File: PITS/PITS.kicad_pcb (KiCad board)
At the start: 2 copper layers, 65 x 30 mm, 56 parts, among them P1 CONN_02X20, P10 I2C, P11 I2C, P12 I2C, P13 I2C, P14 BATT, P2 BNC, P3 BNC, P4 BNC, P5 BNC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

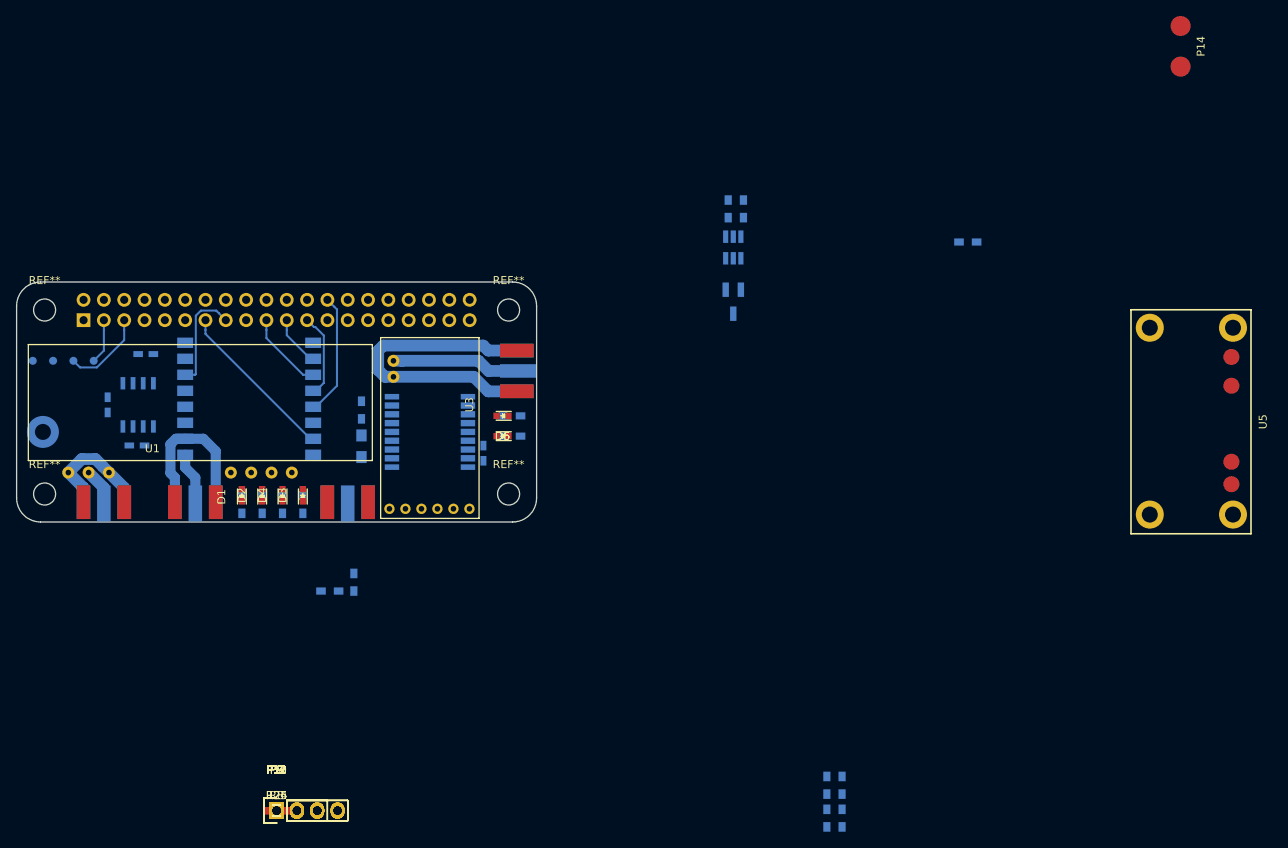
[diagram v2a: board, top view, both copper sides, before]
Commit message: layout - work in progress - power net
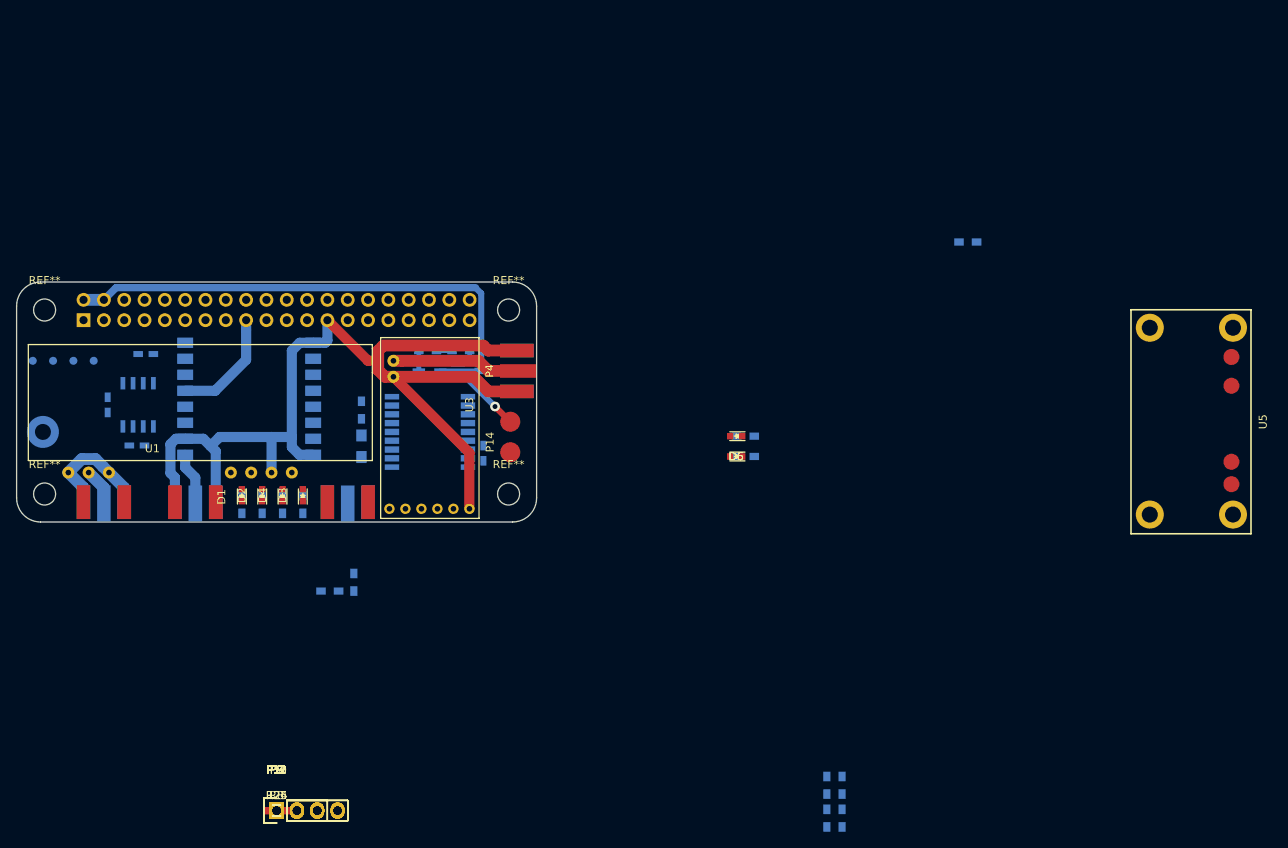
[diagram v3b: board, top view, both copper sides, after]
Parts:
- P14: footprint Connectors:SMD_2 -> Connectors:SMD_2_small
- P4: moved to F.Cu
- moved P14 94.8 mm to (116.7, 66.5), turned to 270 degrees
- moved R6 41.5 mm to (106.4, 57.6), turned to 0 degrees
- moved Q2 41.0 mm to (106.6, 60.1), turned to 0 degrees
- moved R19 39.5 mm to (110.5, 57.6), turned to 180 degrees
- moved Q1 34.1 mm to (111.6, 60.1), turned to 90 degrees
- moved D5 29.3 mm to (144.9, 70.8)
- moved R22 29.3 mm to (146.1, 70.8)
- moved D6 29.3 mm to (144.9, 68.3)
- moved R23 29.3 mm to (146.1, 68.3)
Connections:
- P14 pad 1: +BATT -> +5V_PSU
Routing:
- net GND: track 74.6 -> 143.2 mm
- net +5V: track 0.00 -> 65.5 mm
- net /GPIO27: track 20.6 -> 0.00 mm
- net /GPIO7(CE1): track 15.3 -> 0.00 mm
- net +3V3: track 0.00 -> 14.2 mm
- net /GPIO22: track 13.2 -> 0.00 mm
- net +5V_PSU: track 0.00 -> 11.0 mm, vias 0 -> 1
- net /GPIO3(SCL1): track 10.6 -> 0.00 mm
- net /GPIO11(SCLK0): track 10.6 -> 0.00 mm
- net /GPIO10(MOSI0): track 9.98 -> 0.00 mm
- net /GPIO9(MISO0): track 6.40 -> 0.00 mm
- net /GPIO2(SDA1): track 5.61 -> 0.00 mm
- net Net-(Q1-Pad2): track 0.00 -> 5.05 mm
- net Net-(Q2-Pad1): track 0.00 -> 3.49 mm

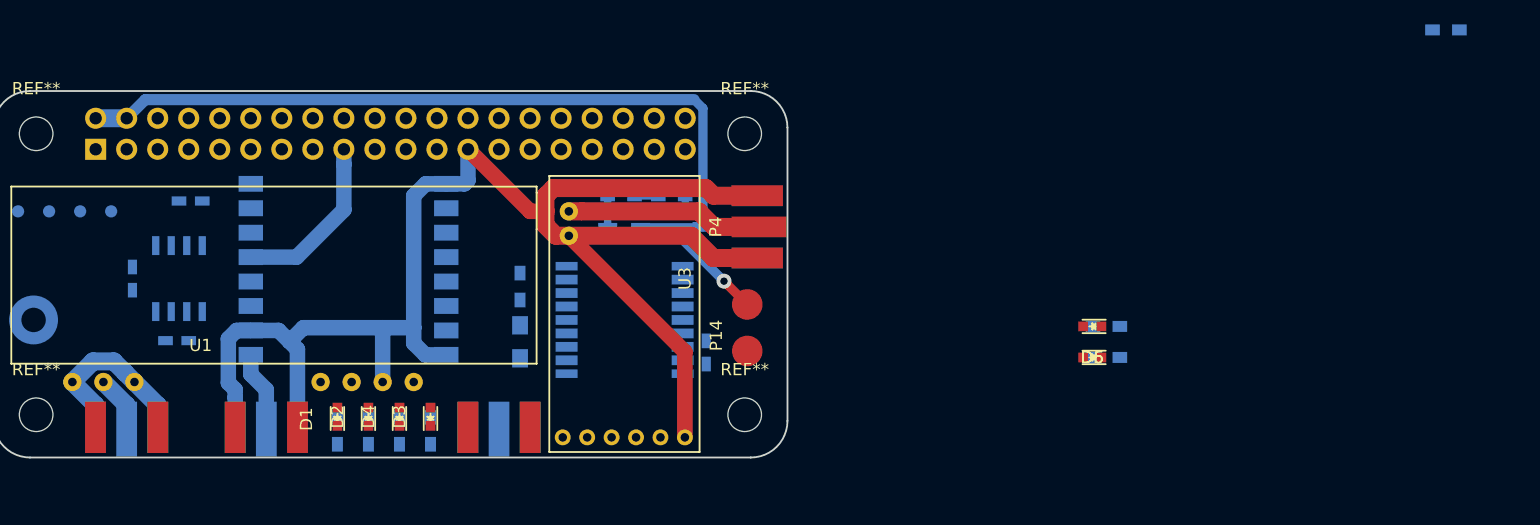
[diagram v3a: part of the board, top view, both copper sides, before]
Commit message: layout - work in progress - first digital nets
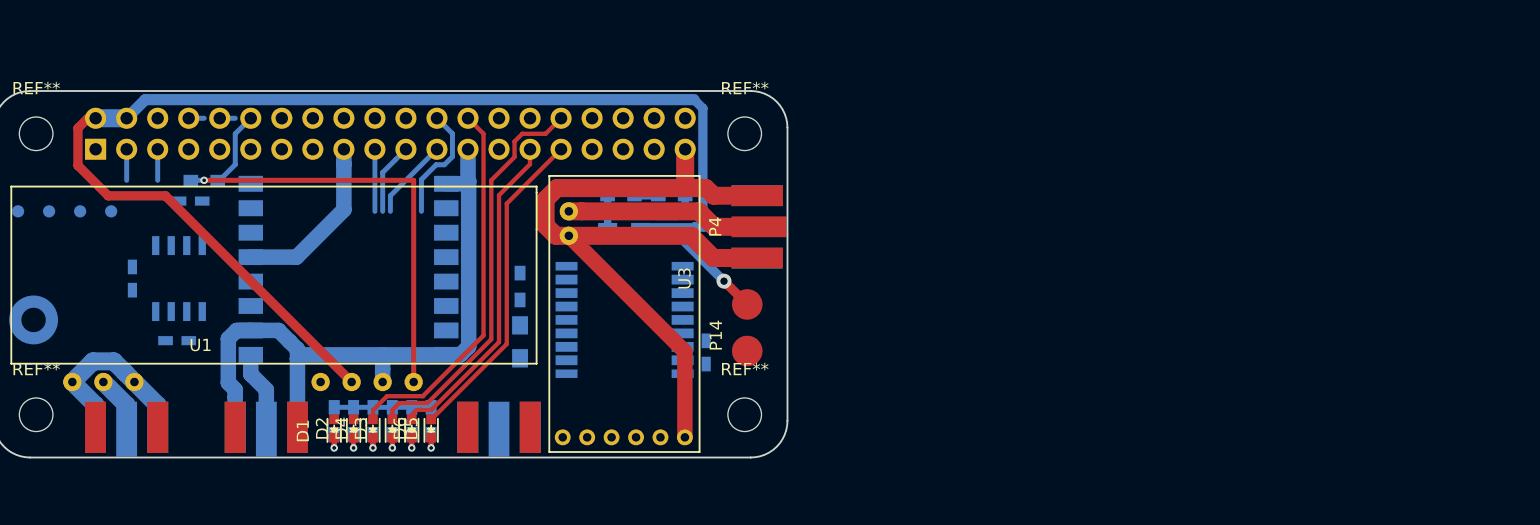
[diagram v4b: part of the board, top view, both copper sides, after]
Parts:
- moved R26 102.4 mm to (72.3, 56.3), turned to 180 degrees
- moved R22 57.1 mm to (89.2, 76.0), turned to 90 degrees
- moved D5 56.0 mm to (89.2, 76.6), turned to 90 degrees
- moved R23 55.8 mm to (90.8, 76.0), turned to 90 degrees
- moved D6 54.8 mm to (90.8, 76.6), turned to 90 degrees
- moved D3 3.27 mm to (87.7, 76.6)
- moved R20 3.23 mm to (87.7, 76.0)
- moved D4 2.38 mm to (86.1, 76.6)
- moved R21 2.32 mm to (86.1, 76.0)
- moved D2 1.56 mm to (84.5, 76.6)
- moved R15 1.47 mm to (84.5, 76.0)
- moved D1 1.01 mm to (82.9, 76.6)
- moved R14 0.86 mm to (82.9, 76.0)
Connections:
- D1 pad 1: GND -> /D1
- D1 pad 2: /D1 -> Net-(D1-Pad2)
- D2 pad 1: GND -> /D2
- D2 pad 2: /D2 -> Net-(D2-Pad2)
- D3 pad 1: GND -> /D3
- D3 pad 2: /D3 -> /GPIO12
- D4 pad 1: GND -> /D4
- D4 pad 2: /D4 -> /GPIO7(CE1)
- D5 pad 1: GND -> /D5
- D5 pad 2: /D5 -> /GPIO5
- D6 pad 1: GND -> /D6
- D6 pad 2: /D6 -> /GPIO6
- P1 pad 16: (no net) -> /GPIO23
- P1 pad 18: (no net) -> /GPIO24
- P1 pad 24: (no net) -> /GPIO8(CE0)
- P1 pad 27: (no net) -> /GPIO0(ID_SD)
- P1 pad 28: (no net) -> /GPIO1(ID_SC)
- R14 pad 1: /GPIO5 -> /D1
- R14 pad 2: /D1 -> GND
- R15 pad 1: /GPIO6 -> /D2
- R15 pad 2: /D2 -> GND
- R20 pad 1: /GPIO20(MOSI1) -> /D3
- R20 pad 2: /D3 -> GND
- R21 pad 1: /GPIO13 -> /D4
- R21 pad 2: /D4 -> GND
- R22 pad 1: /GPIO26 -> /D5
- R22 pad 2: /D5 -> GND
- R23 pad 1: /GPIO21(SCLK1) -> /D6
- R23 pad 2: /D6 -> GND
- U2 pad 13: (no net) -> Net-(U2-Pad13)
- U2 pad 15: (no net) -> Net-(U2-Pad15)
- U2 pad 18: (no net) -> Net-(U2-Pad18)
- U2 pad 5: (no net) -> Net-(U2-Pad5)
- U3 pad 6: (no net) -> Net-(U3-Pad6)
- U3 pad 7: (no net) -> Net-(U3-Pad7)
- U4 pad 11: (no net) -> Net-(U4-Pad11)
- U4 pad 12: (no net) -> Net-(U4-Pad12)
- U4 pad 15: (no net) -> Net-(U4-Pad15)
- U4 pad 16: (no net) -> Net-(U4-Pad16)
- U4 pad 6: (no net) -> Net-(U4-Pad6)
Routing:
- net /HX1-TXD: track 0.00 -> 34.8 mm, vias 0 -> 1
- net +5V: track 65.5 -> 100.1 mm
- net /GPIO12: track 0.00 -> 32.8 mm
- net /GPIO7(CE1): track 0.00 -> 30.6 mm
- net /GPIO5: track 0.00 -> 26.8 mm
- net /GPIO6: track 0.00 -> 26.5 mm
- net /GPIO8(CE0): track 0.00 -> 9.59 mm
- net /GPIO11(SCLK0): track 0.00 -> 6.66 mm
- net /GPIO18: track 0.00 -> 6.29 mm
- net /GPIO9(MISO0): track 0.00 -> 5.87 mm
- net /GPIO10(MOSI0): track 0.00 -> 5.08 mm
- net /GPIO3(SCL1): track 0.00 -> 2.54 mm
- net /GPIO2(SDA1): track 0.00 -> 2.54 mm
- net /D6: track 0.00 -> 1.96 mm, vias 0 -> 1
- net /D5: track 0.00 -> 1.96 mm, vias 0 -> 1
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
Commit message: layout - work in progress - backup GPS antenne change
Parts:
- moved L1 1.45 mm to (99.6, 69.5)
- moved R1 1.14 mm to (99.2, 65.0)
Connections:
- D1 pad 2: Net-(D1-Pad2) -> /GPIO22
- D2 pad 2: Net-(D2-Pad2) -> /GPIO24
- U4 pad 14: /GPIO22 -> /GPIO23
- U4 pad 5: /GPIO7(CE1) -> /GPIO8(CE0)
- U4 pad 7: /GPIO27 -> /GPIO25
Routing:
- net /HX1-TXD: track 34.8 -> 1.09 mm
- net /GPIO24: track 0.00 -> 29.0 mm, vias 0 -> 1
- net /GPIO22: track 0.00 -> 25.5 mm, vias 0 -> 3
- net /GPIO25: track 0.00 -> 20.6 mm
- net /GPIO23: track 0.00 -> 13.1 mm
- net /GPIO10(MOSI0): track 5.08 -> 12.6 mm, vias 0 -> 2
- net /GPIO8(CE0): track 9.59 -> 15.4 mm
- net /GPIO11(SCLK0): track 6.66 -> 11.0 mm
- net /GPIO9(MISO0): track 5.87 -> 8.09 mm, vias 0 -> 2
- net /GPIO6: track 26.5 -> 27.1 mm, vias 0 -> 1
- net /GPIO5: track 26.8 -> 27.3 mm, vias 0 -> 1
- net /GPIO7(CE1): track 30.6 -> 30.2 mm, vias 0 -> 1
- net /GPIO12: track 32.8 -> 32.7 mm, vias 0 -> 1

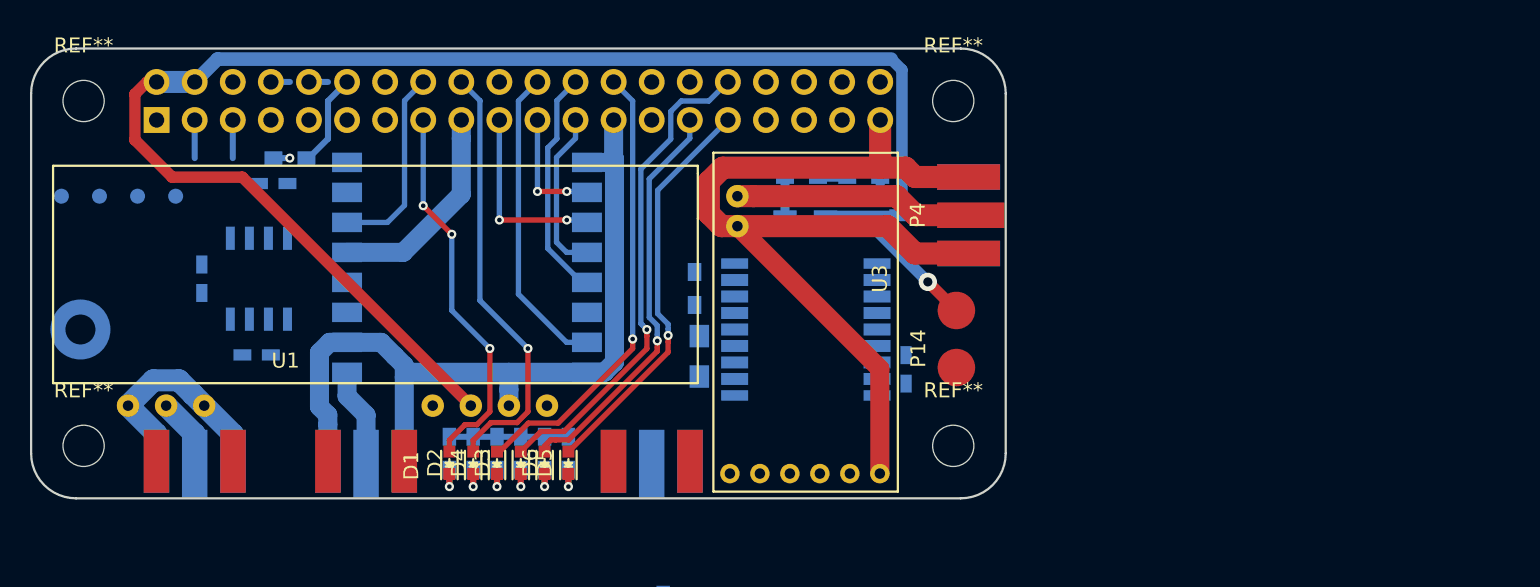
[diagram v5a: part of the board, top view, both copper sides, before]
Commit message: layout - work in progress - RFM, LEDs, UBLOX
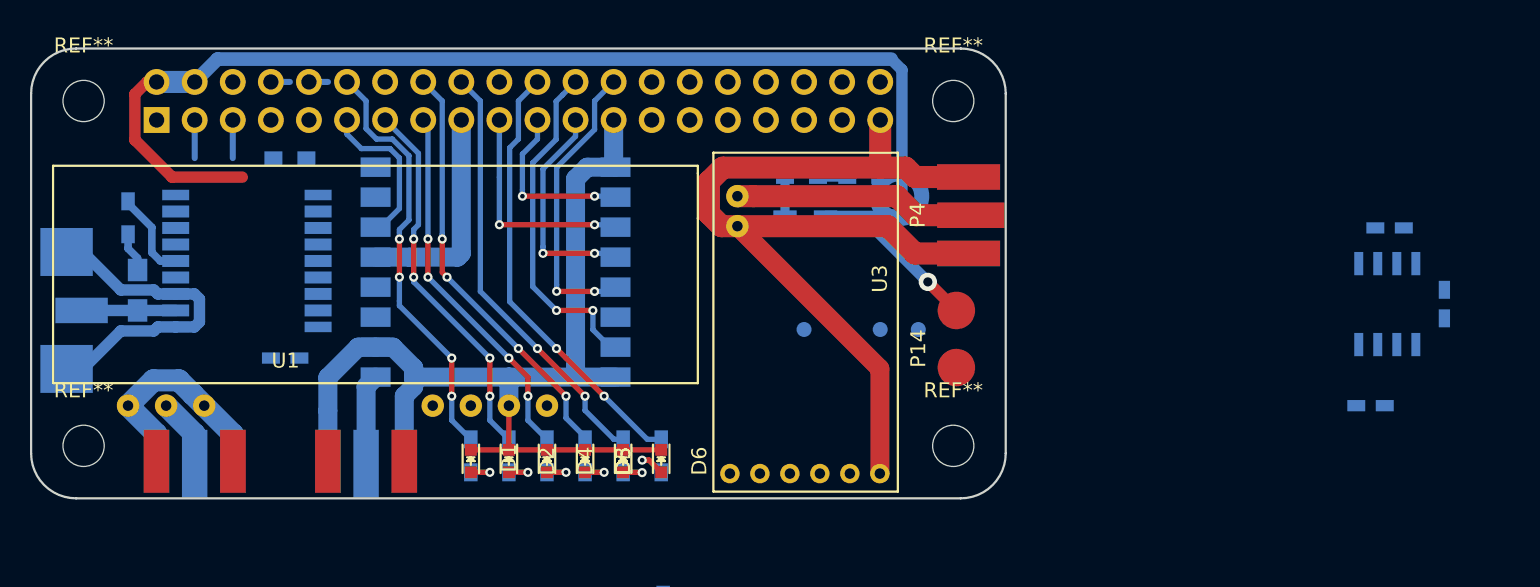
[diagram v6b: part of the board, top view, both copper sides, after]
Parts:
- P2: footprint Connectors:SMA_Edge_small -> RF_Modules:MWSL1252
- moved C1 82.9 mm to (149.3, 66.0), turned to 270 degrees
- moved C2 76.0 mm to (145.6, 61.0), turned to 0 degrees
- moved U7 75.3 mm to (145.4, 66.0), turned to 270 degrees
- moved C4 74.7 mm to (144.3, 72.8), turned to 180 degrees
- moved U8 57.8 mm to (114.2, 67.7), turned to 180 degrees
- moved P2 42.5 mm to (55.1, 66.5), turned to 270 degrees
- moved C14 41.4 mm to (71.9, 69.6), turned to 180 degrees
- moved R1 38.1 mm to (61.5, 60.3)
- moved L1 37.7 mm to (62.1, 65.1)
- moved U2 37.6 mm to (74.1, 58.8)
- moved R23 6.19 mm to (97.0, 76.2), turned to 270 degrees
- moved D6 6.19 mm to (97.0, 76.5), turned to 270 degrees
- moved R22 5.24 mm to (94.5, 76.2), turned to 270 degrees
- moved D5 5.24 mm to (94.5, 76.5), turned to 270 degrees
- moved R20 4.29 mm to (91.9, 76.2), turned to 270 degrees
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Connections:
- D1 pad 1: /D1 -> GND
- D1 pad 2: /GPIO22 -> /D1
- D2 pad 1: /D2 -> GND
- D2 pad 2: /GPIO24 -> /D2
- D3 pad 1: /D3 -> GND
- D3 pad 2: /GPIO12 -> /D3
- D4 pad 1: /D4 -> GND
- D4 pad 2: /GPIO7(CE1) -> /D4
- D5 pad 1: /D5 -> GND
- D5 pad 2: /GPIO5 -> /D5
- D6 pad 1: /D6 -> GND
- D6 pad 2: /GPIO6 -> /D6
- R14 pad 1: /D1 -> /GPIO18
- R14 pad 2: GND -> /D1
- R15 pad 1: /D2 -> /GPIO27
- R15 pad 2: GND -> /D2
- R20 pad 1: /D3 -> /GPIO23
- R20 pad 2: GND -> /D3
- R21 pad 1: /D4 -> /GPIO22
- R21 pad 2: GND -> /D4
- R22 pad 1: /D5 -> /GPIO24
- R22 pad 2: GND -> /D5
- R23 pad 1: /D6 -> /GPIO25
- R23 pad 2: GND -> /D6
- R26 pad 1: /GPIO18 -> /GPIO13
- U3 pad 4: /GPIO17 -> Net-(U3-Pad4)
- U4 pad 14: /GPIO23 -> /GPIO17
- U4 pad 5: /GPIO8(CE0) -> /GPIO7(CE1)
- U4 pad 7: /GPIO25 -> /GPIO8(CE0)
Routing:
- net /GPIO12: track 32.7 -> 0.00 mm, vias 1 -> 0
- net GND: track 142.7 -> 171.0 mm
- net /GPIO5: track 27.3 -> 0.00 mm, vias 1 -> 0
- net /GPIO6: track 27.1 -> 0.00 mm, vias 1 -> 0
- net /GPIO27: track 0.00 -> 25.0 mm, vias 0 -> 4
- net /GPIO18: track 6.29 -> 28.4 mm, vias 0 -> 4
- net +5V: track 100.1 -> 78.5 mm
- net /GPIO23: track 13.1 -> 28.3 mm, vias 0 -> 4
- net /GPIO7(CE1): track 30.2 -> 19.6 mm, vias 1 -> 2
- net /GPIO17: track 0.00 -> 10.6 mm
- net /GPIO25: track 20.6 -> 29.3 mm, vias 0 -> 2
- net /GPIO8(CE0): track 15.4 -> 22.8 mm, vias 0 -> 2
- net Net-(L1-Pad1): track 0.00 -> 6.27 mm
- net Net-(R1-Pad1): track 0.00 -> 5.89 mm
- net /GPIO11(SCLK0): track 11.0 -> 14.7 mm, vias 0 -> 2
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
